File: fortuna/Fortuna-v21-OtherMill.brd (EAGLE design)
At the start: 66 x 55.9 mm, 41 parts, among them IC1 OPA4340P, J1 5V, J2 GND, J3 A0, J4 A3, J5 A5, J6 D2, J7 *D5, J8 *D10, J9 VIN, M1 MOTOR20MM, M2 MOTOR20MM, Q1 PN2222A, Q2 PN2222A

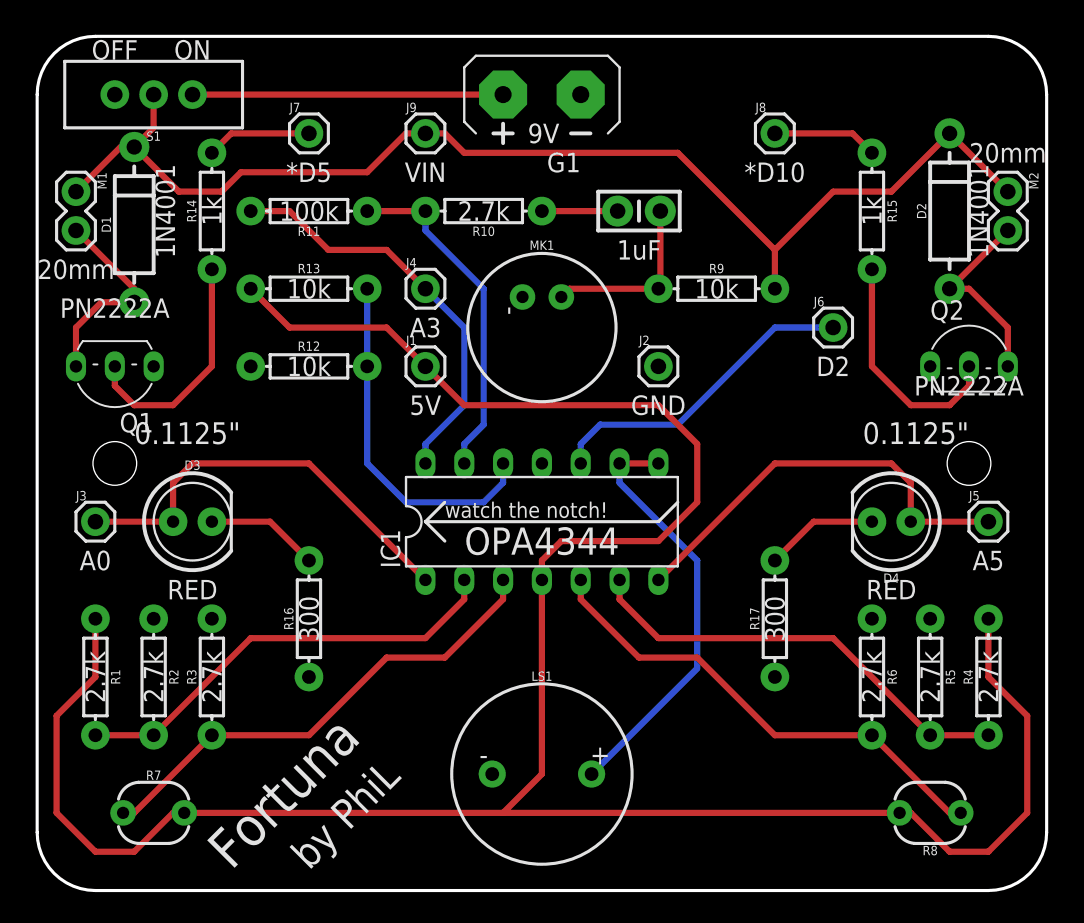
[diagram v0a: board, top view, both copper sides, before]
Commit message: Make major bottom layer (see description)
Since OtherMill just mills the board but doesn't pour copper over the
holes. The top and the bottom layer of a vias are disconnected. In order
to reduce the hard word in soldering, I brough all traces to the bottom
layer & set copper pour for both sides of the board.
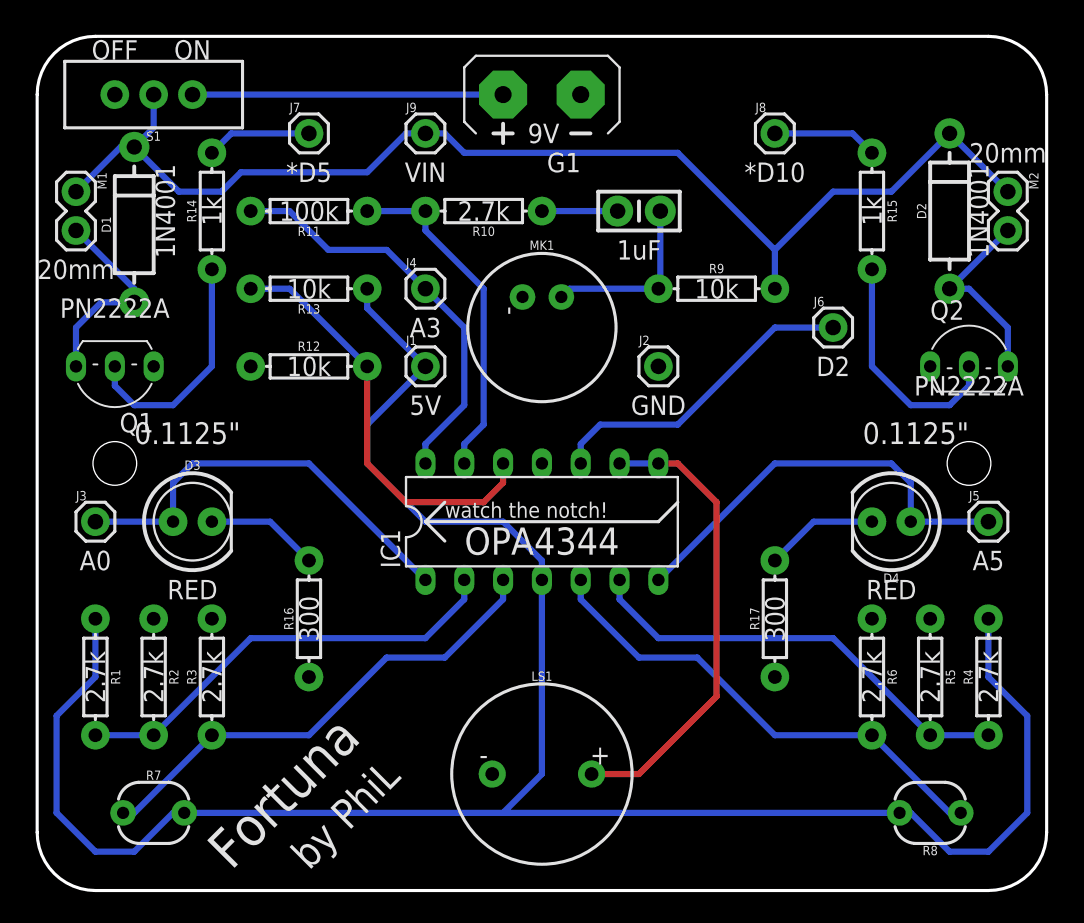
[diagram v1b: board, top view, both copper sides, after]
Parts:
- turned R13 to 180 degrees
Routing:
- net 5V: track 161.7 -> 141.4 mm
- net +MIC: track 23.2 -> 27.8 mm
- net OUT_BUZZER: track 27.8 -> 30.4 mm
- net OUT_MIC: track 27.7 -> 27.1 mm
- added copper zone on layer 1, net GND
